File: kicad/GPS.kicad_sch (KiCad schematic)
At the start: 5 parts, among them J1 Conn_01x03_Pin, J2 Conn_01x03_Pin, J3 Conn_01x03_Pin, J4 Conn_01x03_Pin, U2 ATGM332D-5N31

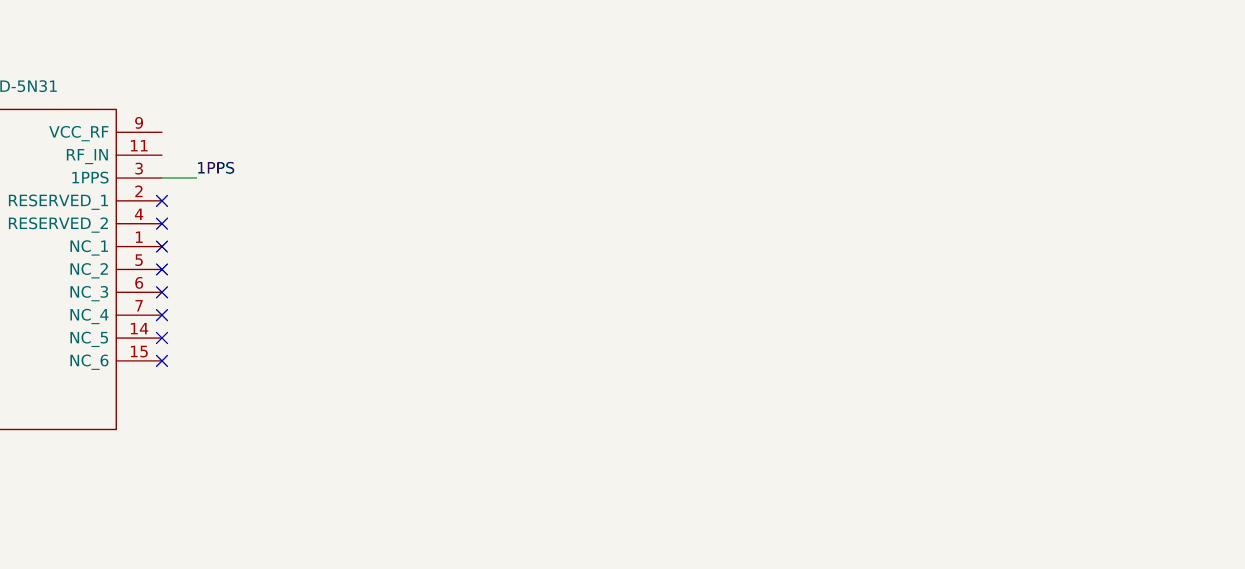
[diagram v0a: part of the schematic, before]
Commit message: [kicad] Added amplifier as well as button for shutdown, added datasheets, changed at2659 package, synced library | TODO: RF-switch
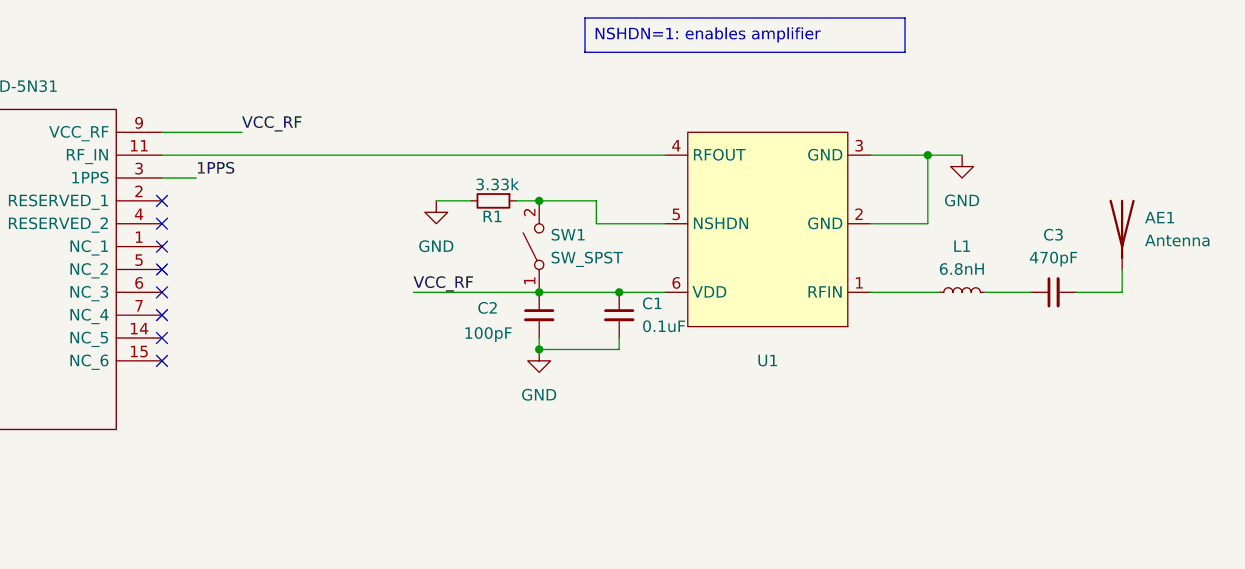
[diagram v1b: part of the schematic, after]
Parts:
- added AE1: Antenna, symbol Device:Antenna
- added C1: 0.1uF, symbol Device:C_Small
- added C2: 100pF, symbol Device:C_Small
- added C3: 470pF, symbol Device:C_Small
- added L1: 6.8nH, symbol Device:L_Small
- added R1: 3.33k, symbol Device:R_Small
- added SW1: SW_SPST, symbol Switch:SW_SPST
- added U1: ~, symbol wireless_testboard:AT2659S
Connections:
- net GND: now also C1.2, C2.2, R1.2, U1.2 (GND), U1.3 (GND)
- net at U2.11 (RF_IN): now also U1.4 (RFOUT)
- net VCC_RF: now reaches U2.9 (VCC_RF)
- net VCC_RF: now also C1.1, C2.1, SW1.1 (A), U1.6 (VDD)
- new net: L1.1, U1.1 (RFIN)
- new net: C3.1, L1.2
- new net: AE1.1 (A), C3.2
- new net: R1.1, SW1.2 (B), U1.5 (NSHDN)

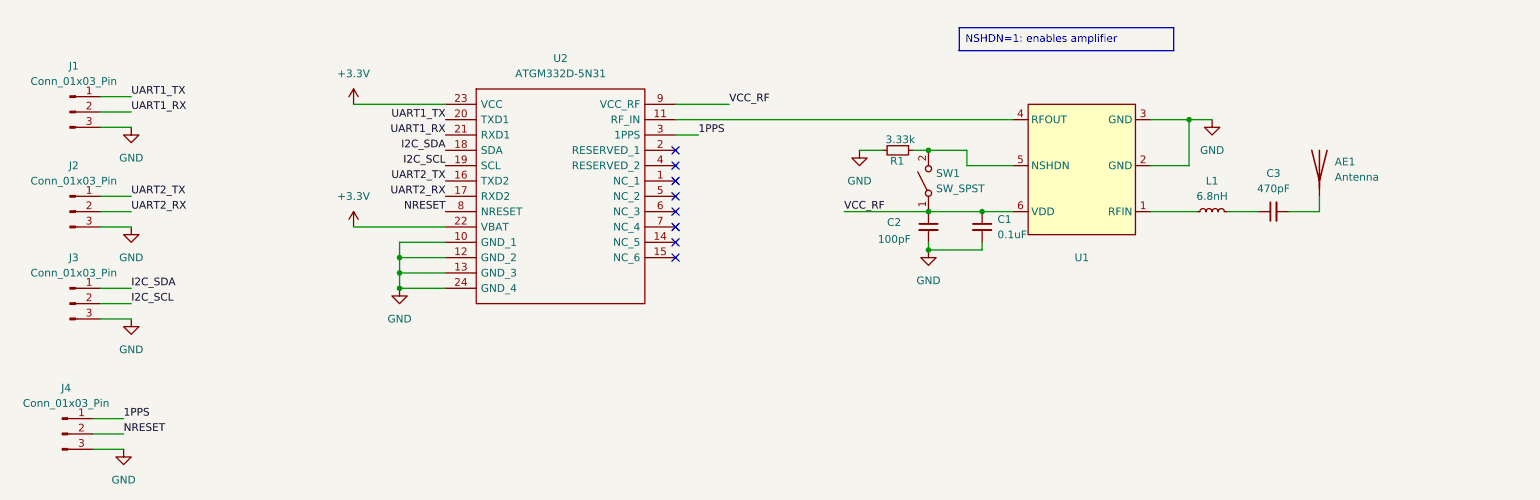
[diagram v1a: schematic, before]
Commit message: added rf switch
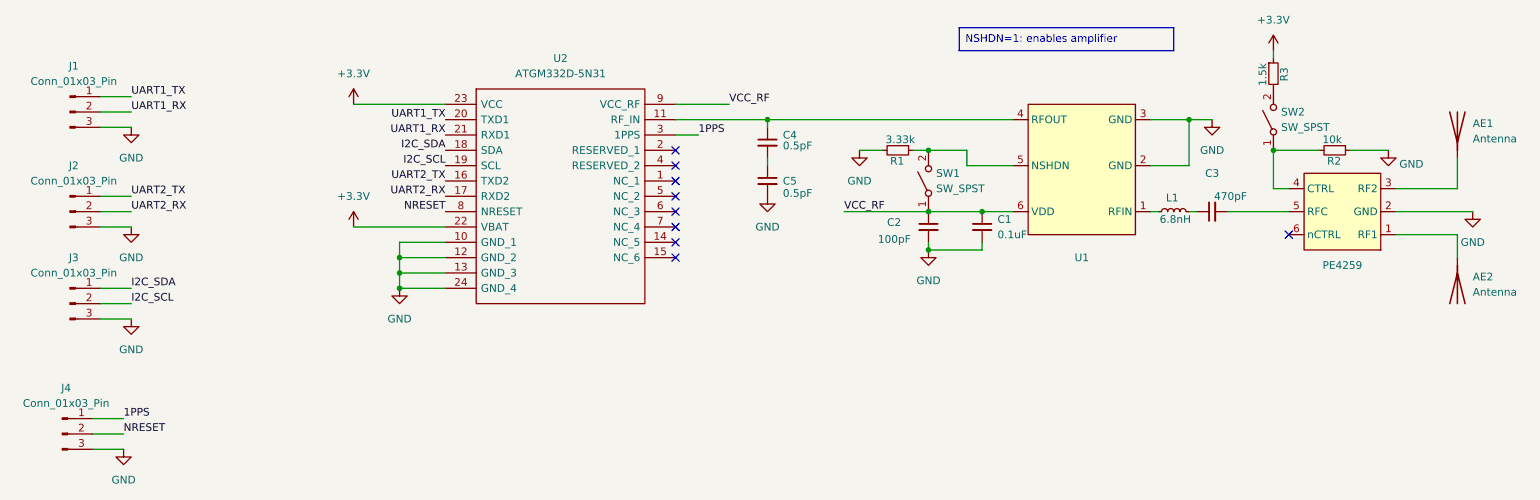
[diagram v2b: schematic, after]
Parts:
- added AE2: Antenna, symbol Device:Antenna
- added C4, C5: 0.5pF, symbol Device:C_Small
- added R2: 10k, symbol Device:R_Small
- added R3: 1.5k, symbol Device:R_Small
- added SW2: SW_SPST, symbol Switch:SW_SPST
- added U3: PE4259, Package_TO_SOT_SMD:SOT-363_SC-70-6_Handsoldering, symbol wireless_testboard:PE4259
- U1: footprint (none) -> Package_TO_SOT_SMD:SOT-23-6; MFR.Part (none) -> AT2659S; jlcpcb (none) -> C883443
- U2: Description_1 Communication Modules/GNSS Modules 12.2x16x2.4mm -> (none); Height 2.6 -> (none); MFR.Partr (none) -> ATGM332D-5N31; Manufacturer_Name ZHONGKEWEI -> (none); Manufacturer_Part_Number ATGM332D-5N31 -> (none)
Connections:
- net +3.3V: now also R3.1
- net GND: now also C5.2, R2.1, U3.2 (GND)
- net at AE1.1 (A): now also U3.3 (RF2); no longer C3.2
- net at U1.4 (RFOUT), U2.11 (RF_IN): now also C4.1
- new net: R2.2, SW2.1 (A), U3.4 (CTRL)
- new net: R3.2, SW2.2 (B)
- new net: AE2.1 (A), U3.1 (RF1)
- new net: C4.2, C5.1
- new net: C3.2, U3.5 (RFC)
- no-connect marks 8 -> 9
